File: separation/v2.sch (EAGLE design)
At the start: 8 parts

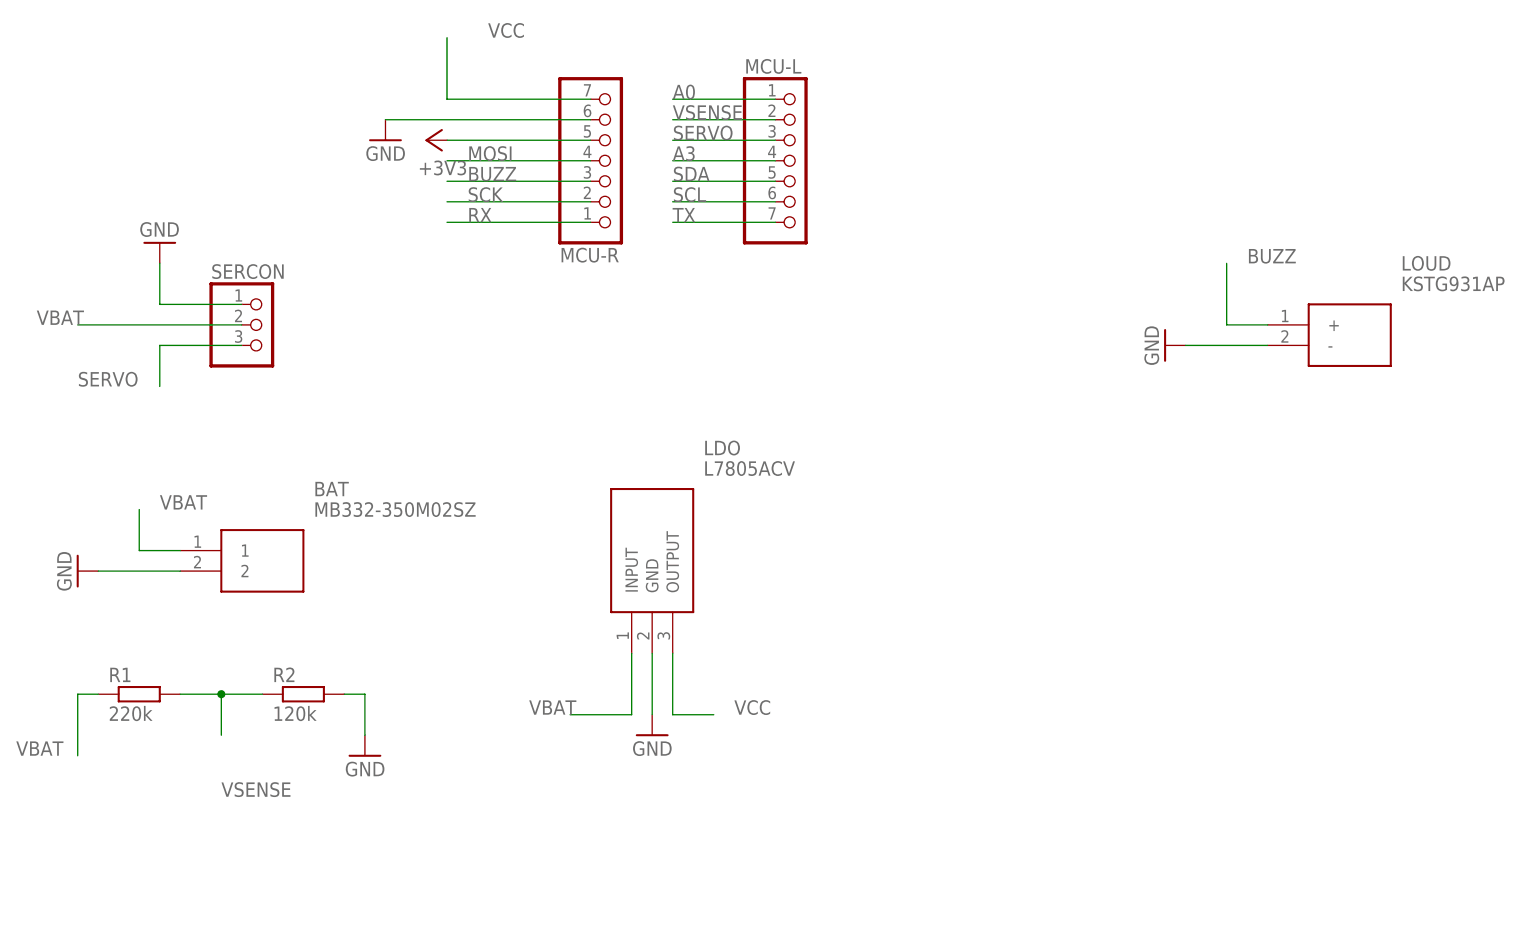
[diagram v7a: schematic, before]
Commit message: add test points for signals with no easy access
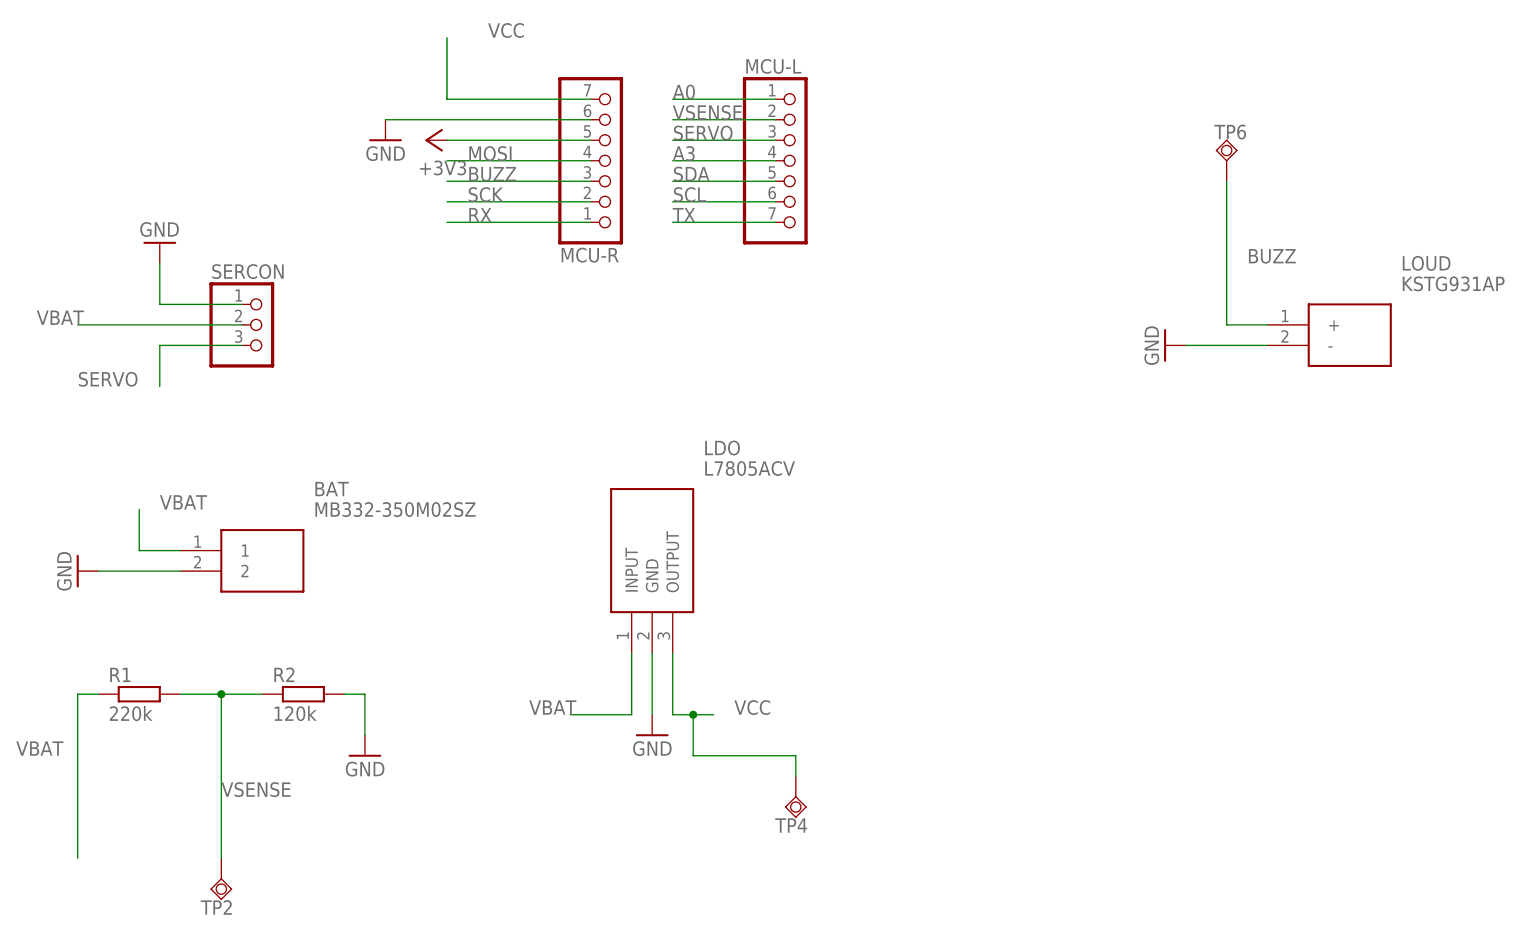
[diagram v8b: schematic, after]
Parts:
- added TP2, TP4, TP6: TPSQB2,54, testpad:TPSQB2,54
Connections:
- net BUZZ: now also TP6.TP
- net VCC: now also TP4.TP
- net VSENSE: now also TP2.TP
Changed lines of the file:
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@@
 <part name="R2" library="rcl" library_urn="urn:adsk.eagle:library:334" deviceset="R-EU_" device="0204/2V" package3d_urn="urn:adsk.eagle:package:23495/1" value="120k"/>
 <part name="GND6" library="supply1" library_urn="urn:adsk.eagle:library:371" deviceset="GND" device=""/>
+<part name="TP2" library="testpad" library_urn="urn:adsk.eagle:library:385" deviceset="TPSQ" device="B2,54" package3d_urn="urn:adsk.eagle:package:27948/1"/>
+<part name="TP4" library="testpad" library_urn="urn:adsk.eagle:library:385" deviceset="TPSQ" device="B2,54" package3d_urn="urn:adsk.eagle:package:27948/1"/>
+<part name="TP6" library="testpad" library_urn="urn:adsk.eagle:library:385" deviceset="TPSQ" device="B2,54" package3d_urn="urn:adsk.eagle:package:27948/1"/>
 </parts>
 <sheets>
@@
 <attribute name="VALUE" x="10.16" y="-17.78" size="1.778" layer="96" rot="MR0"/>
 </instance>
+<instance part="TP2" gate="G$1" x="-10.16" y="-30.48" smashed="yes">
+<attribute name="NAME" x="-12.7" y="-34.925" size="1.778" layer="95"/>
+<attribute name="TP_SIGNAL_NAME" x="-7.62" y="-31.75" size="1.778" layer="97"/>
+</instance>
+<instance part="TP4" gate="G$1" x="60.96" y="-20.32" smashed="yes">
+<attribute name="NAME" x="58.42" y="-24.765" size="1.778" layer="95"/>
+<attribute name="TP_SIGNAL_NAME" x="63.5" y="-21.59" size="1.778" layer="97"/>
+</instance>
+<instance part="TP6" gate="G$1" x="114.3" y="58.42" smashed="yes" rot="R180">
+<attribute name="NAME" x="116.84" y="62.865" size="1.778" layer="95" rot="R180"/>
+<attribute name="TP_SIGNAL_NAME" x="111.76" y="59.69" size="1.778" layer="97" rot="R180"/>
+</instance>
 </instances>
 <busses>
@@
 <pinref part="LDO" gate="G$1" pin="OUTPUT"/>
 <wire x1="45.72" y1="-2.54" x2="45.72" y2="-10.16" width="0.1524" layer="91"/>
-<wire x1="45.72" y1="-10.16" x2="50.8" y2="-10.16" width="0.1524" layer="91"/>
+<wire x1="45.72" y1="-10.16" x2="48.26" y2="-10.16" width="0.1524" layer="91"/>
 <label x="53.34" y="-10.16" size="1.778" layer="95"/>
+<pinref part="TP4" gate="G$1" pin="TP"/>
+<wire x1="48.26" y1="-10.16" x2="50.8" y2="-10.16" width="0.1524" layer="91"/>
+<wire x1="60.96" y1="-17.78" x2="60.96" y2="-15.24" width="0.1524" layer="91"/>
+<wire x1="60.96" y1="-15.24" x2="48.26" y2="-15.24" width="0.1524" layer="91"/>
+<wire x1="48.26" y1="-15.24" x2="48.26" y2="-10.16" width="0.1524" layer="91"/>
+<junction x="48.26" y="-10.16"/>
 </segment>
 </net>
@@
 <pinref part="R1" gate="G$1" pin="1"/>
 <wire x1="-25.4" y1="-7.62" x2="-27.94" y2="-7.62" width="0.1524" layer="91"/>
-<wire x1="-27.94" y1="-7.62" x2="-27.94" y2="-15.24" width="0.1524" layer="91"/>
 <label x="-35.56" y="-15.24" size="1.778" layer="95"/>
+<wire x1="-27.94" y1="-7.62" x2="-27.94" y2="-27.94" width="0.1524" layer="91"/>
 </segment>
 <segment>
@@
 <pinref part="SERCON" gate="A" pin="3"/>
 <wire x1="-7.62" y1="35.56" x2="-17.78" y2="35.56" width="0.1524" layer="91"/>
+<label x="-27.94" y="30.48" size="1.778" layer="95"/>
 <wire x1="-17.78" y1="35.56" x2="-17.78" y2="30.48" width="0.1524" layer="91"/>
-<label x="-27.94" y="30.48" size="1.778" layer="95"/>
 </segment>
 <segment>
@@
 <pinref part="LOUD" gate="G$1" pin="+"/>
 <wire x1="119.38" y1="38.1" x2="114.3" y2="38.1" width="0.1524" layer="91"/>
-<wire x1="114.3" y1="38.1" x2="114.3" y2="45.72" width="0.1524" layer="91"/>
 <label x="116.84" y="45.72" size="1.778" layer="95"/>
+<pinref part="TP6" gate="G$1" pin="TP"/>
+<wire x1="114.3" y1="55.88" x2="114.3" y2="38.1" width="0.1524" layer="91"/>
 </segment>
 <segment>
@@
 <wire x1="-15.24" y1="-7.62" x2="-10.16" y2="-7.62" width="0.1524" layer="91"/>
 <wire x1="-10.16" y1="-7.62" x2="-5.08" y2="-7.62" width="0.1524" layer="91"/>
-<wire x1="-10.16" y1="-7.62" x2="-10.16" y2="-12.7" width="0.1524" layer="91"/>
 <junction x="-10.16" y="-7.62"/>
 <label x="-10.16" y="-20.32" size="1.778" layer="95"/>
-</segment>
-<segment>
+<pinref part="TP2" gate="G$1" pin="TP"/>
+<wire x1="-10.16" y1="-27.94" x2="-10.16" y2="-7.62" width="0.1524" layer="91"/>
+</segment>
+<segment>
